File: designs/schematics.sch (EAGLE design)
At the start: 6 parts

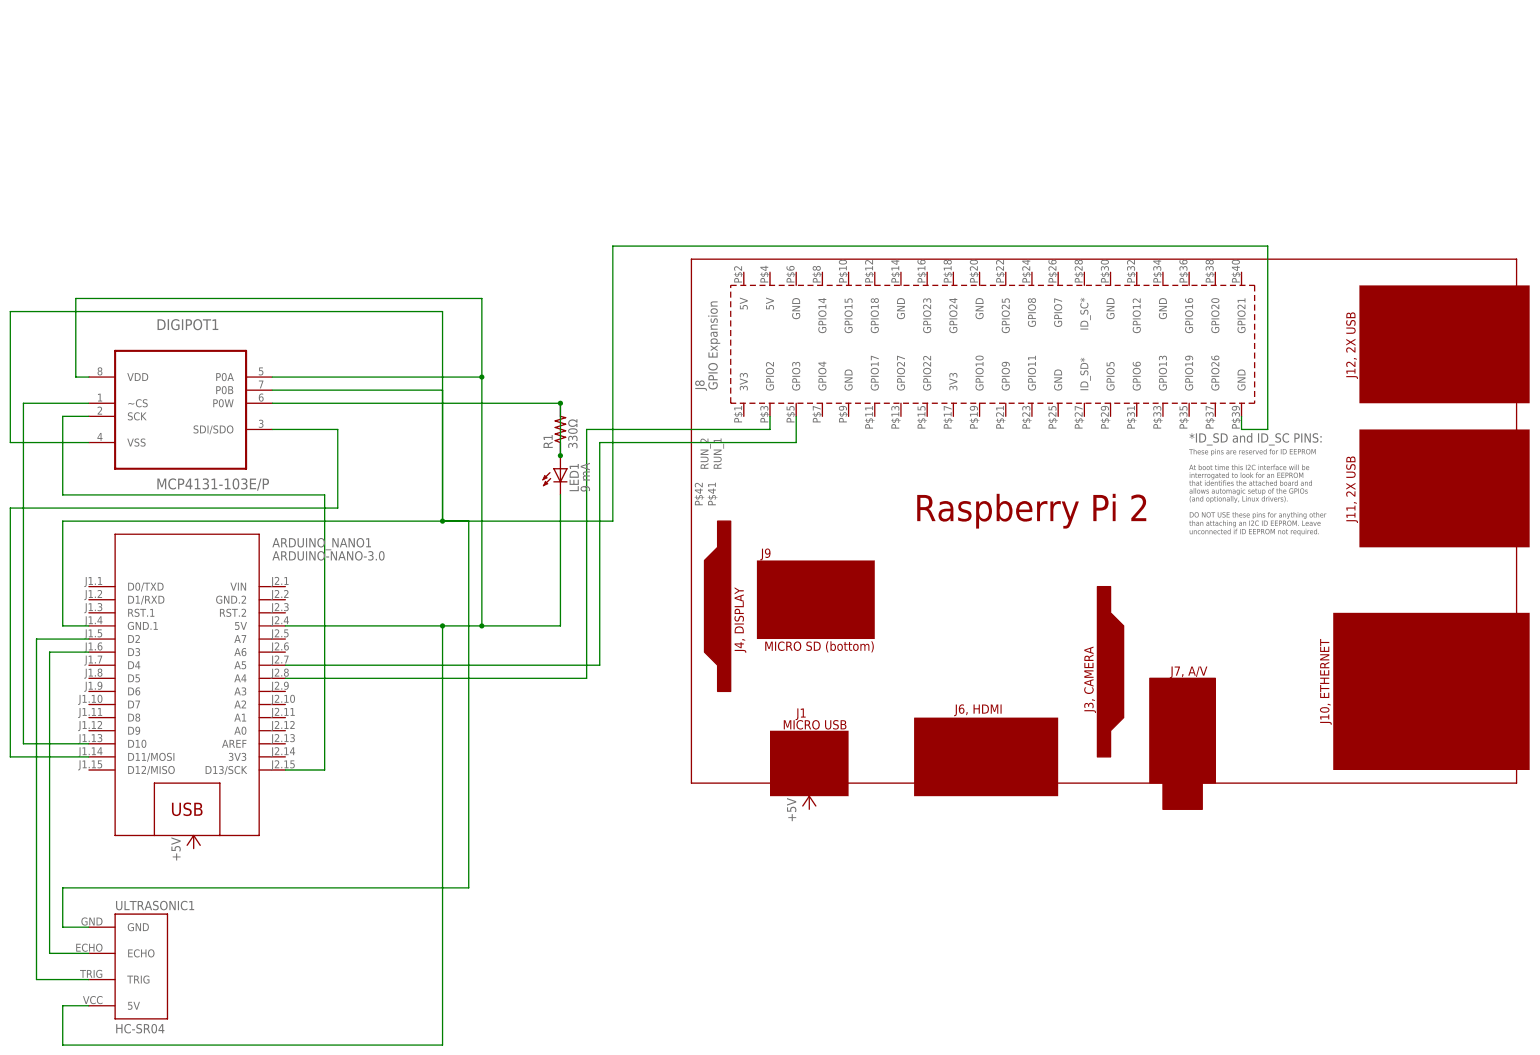
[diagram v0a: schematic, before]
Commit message: ultrasonic moved to pi
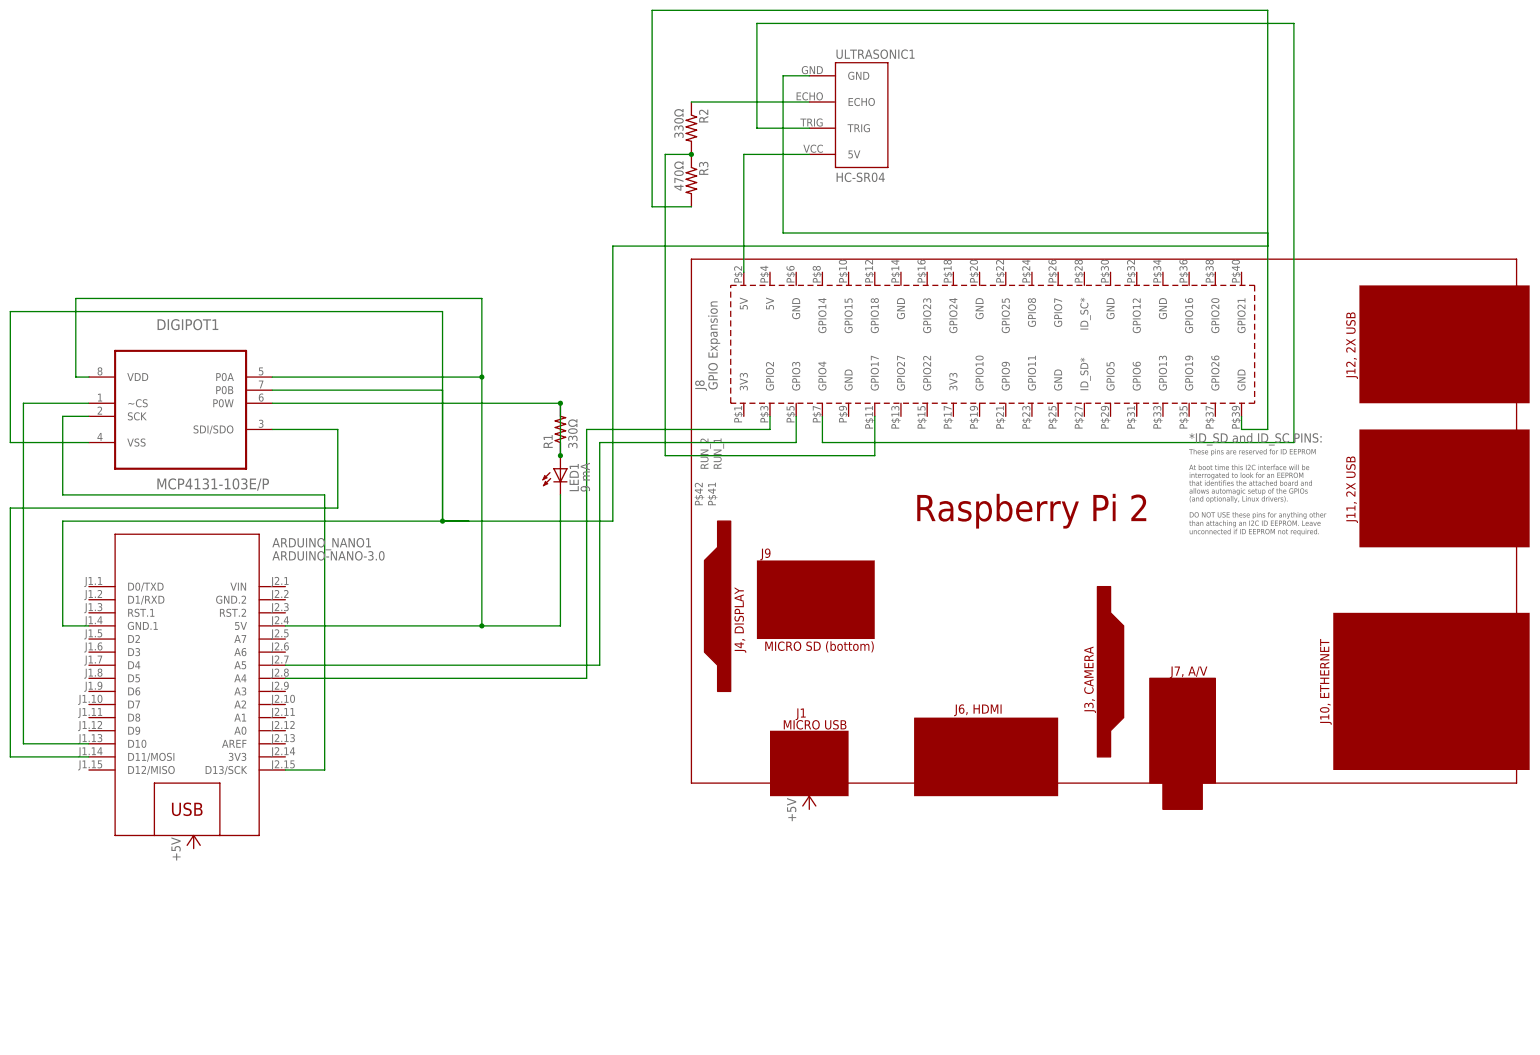
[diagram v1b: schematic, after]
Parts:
- added R2: 330Ω, resistor:R-US_0204/7
- added R3: 470Ω, resistor:R-US_0204/7
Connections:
- new net N$10: R2.1, ULTRASONIC1.ECHO
- new net N$11: R2.2, R3.1, RASPBERRY_PI_TWO1.GPIO17
- net N$1: now also R3.2
- net N$2: now also RASPBERRY_PI_TWO1.5V@2, ULTRASONIC1.5V; no longer ARDUINO_NANO1.D3, ULTRASONIC1.ECHO
- net N$3: now also RASPBERRY_PI_TWO1.GPIO4; no longer ARDUINO_NANO1.D2
- net N$4: no longer ULTRASONIC1.5V
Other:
- moved on the sheet: ULTRASONIC1
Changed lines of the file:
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@@
 <part name="+5V1" library="supply1" library_urn="urn:adsk.eagle:library:371" deviceset="+5V" device=""/>
 <part name="+5V2" library="supply1" library_urn="urn:adsk.eagle:library:371" deviceset="+5V" device=""/>
+<part name="R2" library="resistor" library_urn="urn:adsk.eagle:library:348" deviceset="R-US_" device="0204/7" package3d_urn="urn:adsk.eagle:package:25945/1" value="330Ω"/>
+<part name="R3" library="resistor" library_urn="urn:adsk.eagle:library:348" deviceset="R-US_" device="0204/7" package3d_urn="urn:adsk.eagle:package:25945/1" value="470Ω"/>
 </parts>
 <sheets>
@@
 <instance part="ARDUINO_NANO1" gate="G$1" x="0" y="5.08"/>
 <instance part="RASPBERRY_PI_TWO1" gate="G$1" x="96.52" y="-15.24"/>
-<instance part="ULTRASONIC1" gate="J_ULTRASONIC" x="-7.62" y="-50.8"/>
+<instance part="ULTRASONIC1" gate="J_ULTRASONIC" x="132.08" y="114.3"/>
 <instance part="DIGIPOT1" gate="A" x="-2.54" y="60.96"/>
 <instance part="R1" gate="G$1" x="71.12" y="53.34" rot="R90"/>
@@
 <instance part="+5V1" gate="1" x="0" y="-25.4"/>
 <instance part="+5V2" gate="1" x="119.38" y="-17.78"/>
+<instance part="R2" gate="G$1" x="96.52" y="111.76" rot="R270"/>
+<instance part="R3" gate="G$1" x="96.52" y="101.6" rot="R270"/>
 </instances>
 <busses>
 </busses>
 <nets>
-<net name="N$2" class="0">
-<segment>
-<pinref part="ULTRASONIC1" gate="J_ULTRASONIC" pin="ECHO"/>
-<wire x1="-20.32" y1="-48.26" x2="-27.94" y2="-48.26" width="0.1524" layer="91"/>
-<wire x1="-27.94" y1="-48.26" x2="-27.94" y2="10.16" width="0.1524" layer="91"/>
-<pinref part="ARDUINO_NANO1" gate="G$1" pin="D3"/>
-<wire x1="-27.94" y1="10.16" x2="-20.32" y2="10.16" width="0.1524" layer="91"/>
-</segment>
-</net>
-<net name="N$3" class="0">
-<segment>
-<pinref part="ULTRASONIC1" gate="J_ULTRASONIC" pin="TRIG"/>
-<wire x1="-20.32" y1="-53.34" x2="-30.48" y2="-53.34" width="0.1524" layer="91"/>
-<wire x1="-30.48" y1="-53.34" x2="-30.48" y2="12.7" width="0.1524" layer="91"/>
-<pinref part="ARDUINO_NANO1" gate="G$1" pin="D2"/>
-<wire x1="-30.48" y1="12.7" x2="-20.32" y2="12.7" width="0.1524" layer="91"/>
-</segment>
-</net>
 <net name="N$5" class="0">
 <segment>
@@
 <wire x1="-25.4" y1="35.56" x2="48.26" y2="35.56" width="0.1524" layer="91"/>
 <junction x="48.26" y="35.56"/>
-<pinref part="ULTRASONIC1" gate="J_ULTRASONIC" pin="GND"/>
-<wire x1="-20.32" y1="-43.18" x2="-25.4" y2="-43.18" width="0.1524" layer="91"/>
-<wire x1="-25.4" y1="-43.18" x2="-25.4" y2="-35.56" width="0.1524" layer="91"/>
-<wire x1="-25.4" y1="-35.56" x2="53.34" y2="-35.56" width="0.1524" layer="91"/>
-<wire x1="53.34" y1="-35.56" x2="53.34" y2="35.56" width="0.1524" layer="91"/>
 <wire x1="53.34" y1="35.56" x2="48.26" y2="35.56" width="0.1524" layer="91"/>
 <pinref part="DIGIPOT1" gate="A" pin="VSS"/>
@@
 <wire x1="81.28" y1="88.9" x2="81.28" y2="35.56" width="0.1524" layer="91"/>
 <wire x1="81.28" y1="35.56" x2="48.26" y2="35.56" width="0.1524" layer="91"/>
+<pinref part="ULTRASONIC1" gate="J_ULTRASONIC" pin="GND"/>
+<wire x1="119.38" y1="121.92" x2="114.3" y2="121.92" width="0.1524" layer="91"/>
+<wire x1="114.3" y1="121.92" x2="114.3" y2="91.44" width="0.1524" layer="91"/>
+<wire x1="114.3" y1="91.44" x2="208.28" y2="91.44" width="0.1524" layer="91"/>
+<wire x1="208.28" y1="91.44" x2="208.28" y2="88.9" width="0.1524" layer="91"/>
+<pinref part="R3" gate="G$1" pin="2"/>
+<wire x1="96.52" y1="96.52" x2="88.9" y2="96.52" width="0.1524" layer="91"/>
+<wire x1="88.9" y1="96.52" x2="88.9" y2="134.62" width="0.1524" layer="91"/>
+<wire x1="88.9" y1="134.62" x2="208.28" y2="134.62" width="0.1524" layer="91"/>
+<wire x1="208.28" y1="134.62" x2="208.28" y2="88.9" width="0.1524" layer="91"/>
 </segment>
 </net>
@@
 <segment>
 <pinref part="ARDUINO_NANO1" gate="G$1" pin="5V"/>
-<wire x1="17.78" y1="15.24" x2="48.26" y2="15.24" width="0.1524" layer="91"/>
-<junction x="48.26" y="15.24"/>
-<pinref part="ULTRASONIC1" gate="J_ULTRASONIC" pin="5V"/>
-<wire x1="-20.32" y1="-58.42" x2="-25.4" y2="-58.42" width="0.1524" layer="91"/>
-<wire x1="-25.4" y1="-58.42" x2="-25.4" y2="-66.04" width="0.1524" layer="91"/>
-<wire x1="-25.4" y1="-66.04" x2="48.26" y2="-66.04" width="0.1524" layer="91"/>
-<wire x1="48.26" y1="-66.04" x2="48.26" y2="15.24" width="0.1524" layer="91"/>
+<wire x1="17.78" y1="15.24" x2="55.88" y2="15.24" width="0.1524" layer="91"/>
 <pinref part="DIGIPOT1" gate="A" pin="VDD"/>
 <wire x1="-20.32" y1="63.5" x2="-22.86" y2="63.5" width="0.1524" layer="91"/>
@@
 <wire x1="-22.86" y1="78.74" x2="55.88" y2="78.74" width="0.1524" layer="91"/>
 <wire x1="55.88" y1="78.74" x2="55.88" y2="63.5" width="0.1524" layer="91"/>
-<wire x1="55.88" y1="15.24" x2="48.26" y2="15.24" width="0.1524" layer="91"/>
 <pinref part="DIGIPOT1" gate="A" pin="P0A"/>
 <wire x1="15.24" y1="63.5" x2="55.88" y2="63.5" width="0.1524" layer="91"/>
@@
 </segment>
 </net>
+<net name="N$2" class="0">
+<segment>
+<pinref part="ULTRASONIC1" gate="J_ULTRASONIC" pin="5V"/>
+<pinref part="RASPBERRY_PI_TWO1" gate="G$1" pin="5V@2"/>
+<wire x1="119.38" y1="106.68" x2="106.68" y2="106.68" width="0.1524" layer="91"/>
+<wire x1="106.68" y1="106.68" x2="106.68" y2="83.82" width="0.1524" layer="91"/>
+</segment>
+</net>
+<net name="N$3" class="0">
+<segment>
+<pinref part="ULTRASONIC1" gate="J_ULTRASONIC" pin="TRIG"/>
+<wire x1="119.38" y1="111.76" x2="109.22" y2="111.76" width="0.1524" layer="91"/>
+<wire x1="109.22" y1="111.76" x2="109.22" y2="132.08" width="0.1524" layer="91"/>
+<wire x1="109.22" y1="132.08" x2="213.36" y2="132.08" width="0.1524" layer="91"/>
+<wire x1="213.36" y1="132.08" x2="213.36" y2="50.8" width="0.1524" layer="91"/>
+<pinref part="RASPBERRY_PI_TWO1" gate="G$1" pin="GPIO4"/>
+<wire x1="213.36" y1="50.8" x2="121.92" y2="50.8" width="0.1524" layer="91"/>
+<wire x1="121.92" y1="50.8" x2="121.92" y2="55.88" width="0.1524" layer="91"/>
+</segment>
+</net>
+<net name="N$10" class="0">
+<segment>
+<pinref part="ULTRASONIC1" gate="J_ULTRASONIC" pin="ECHO"/>
+<wire x1="119.38" y1="116.84" x2="96.52" y2="116.84" width="0.1524" layer="91"/>
+<pinref part="R2" gate="G$1" pin="1"/>
+</segment>
+</net>
+<net name="N$11" class="0">
+<segment>
+<pinref part="R2" gate="G$1" pin="2"/>
+<wire x1="96.52" y1="106.68" x2="91.44" y2="106.68" width="0.1524" layer="91"/>
+<wire x1="91.44" y1="106.68" x2="91.44" y2="48.26" width="0.1524" layer="91"/>
+<pinref part="RASPBERRY_PI_TWO1" gate="G$1" pin="GPIO17"/>
+<wire x1="91.44" y1="48.26" x2="132.08" y2="48.26" width="0.1524" layer="91"/>
+<wire x1="132.08" y1="48.26" x2="132.08" y2="55.88" width="0.1524" layer="91"/>
+<pinref part="R3" gate="G$1" pin="1"/>
+<junction x="96.52" y="106.68"/>
+</segment>
+</net>
